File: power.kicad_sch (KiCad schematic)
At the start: 38 parts, among them J2 Power, U3 TLV62569DBV, U4 TLV62569DBV, U5 TLV62569DBV

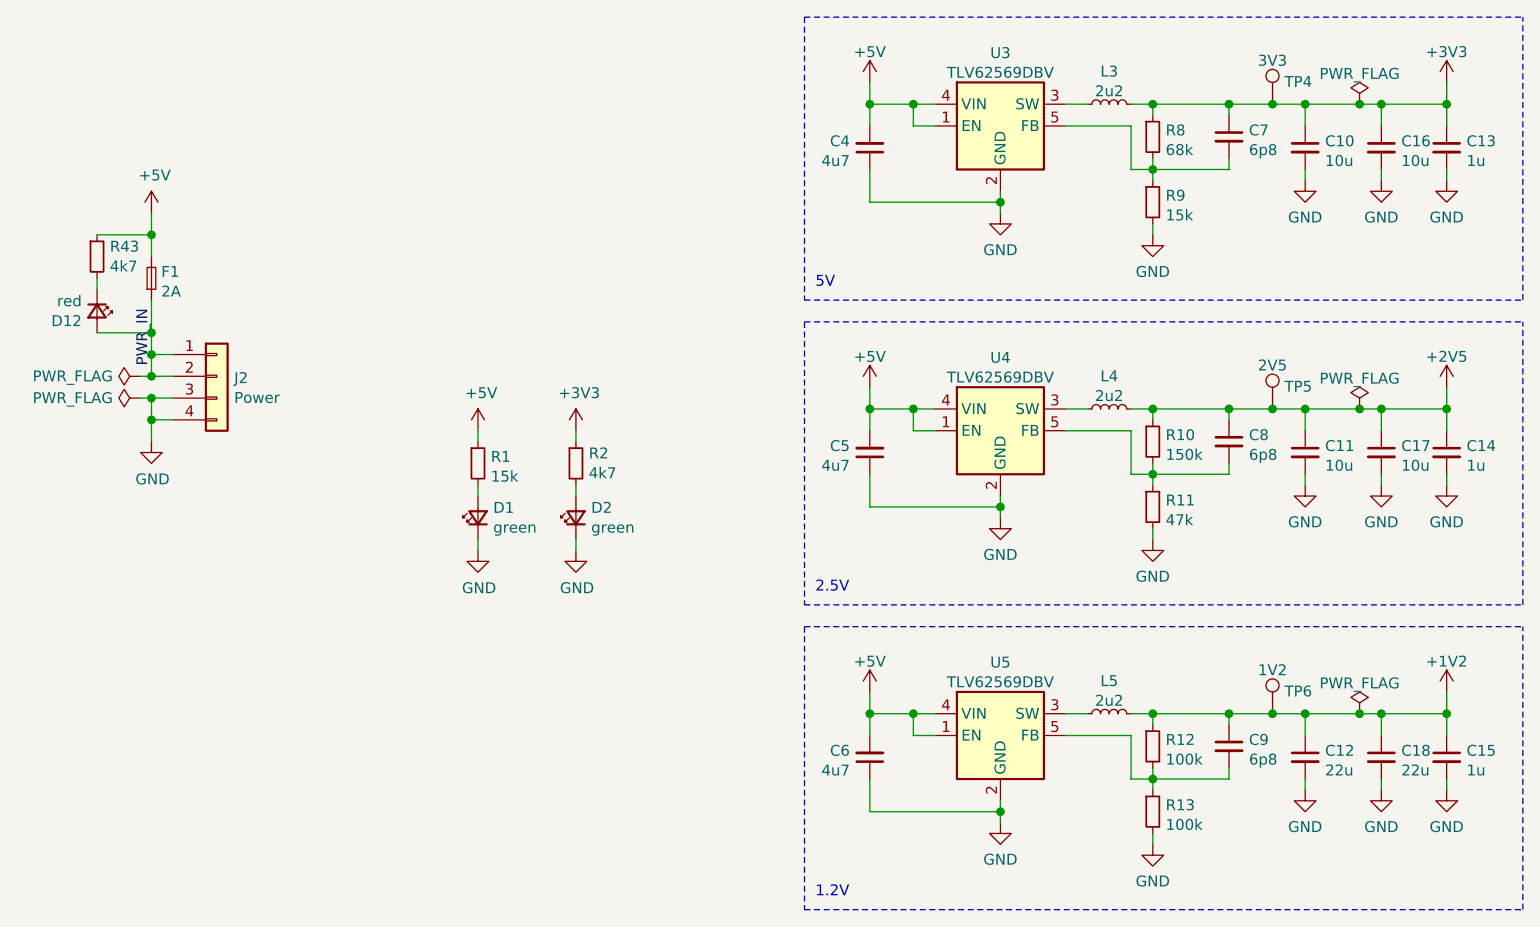
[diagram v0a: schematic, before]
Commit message: Update to KiCad 6
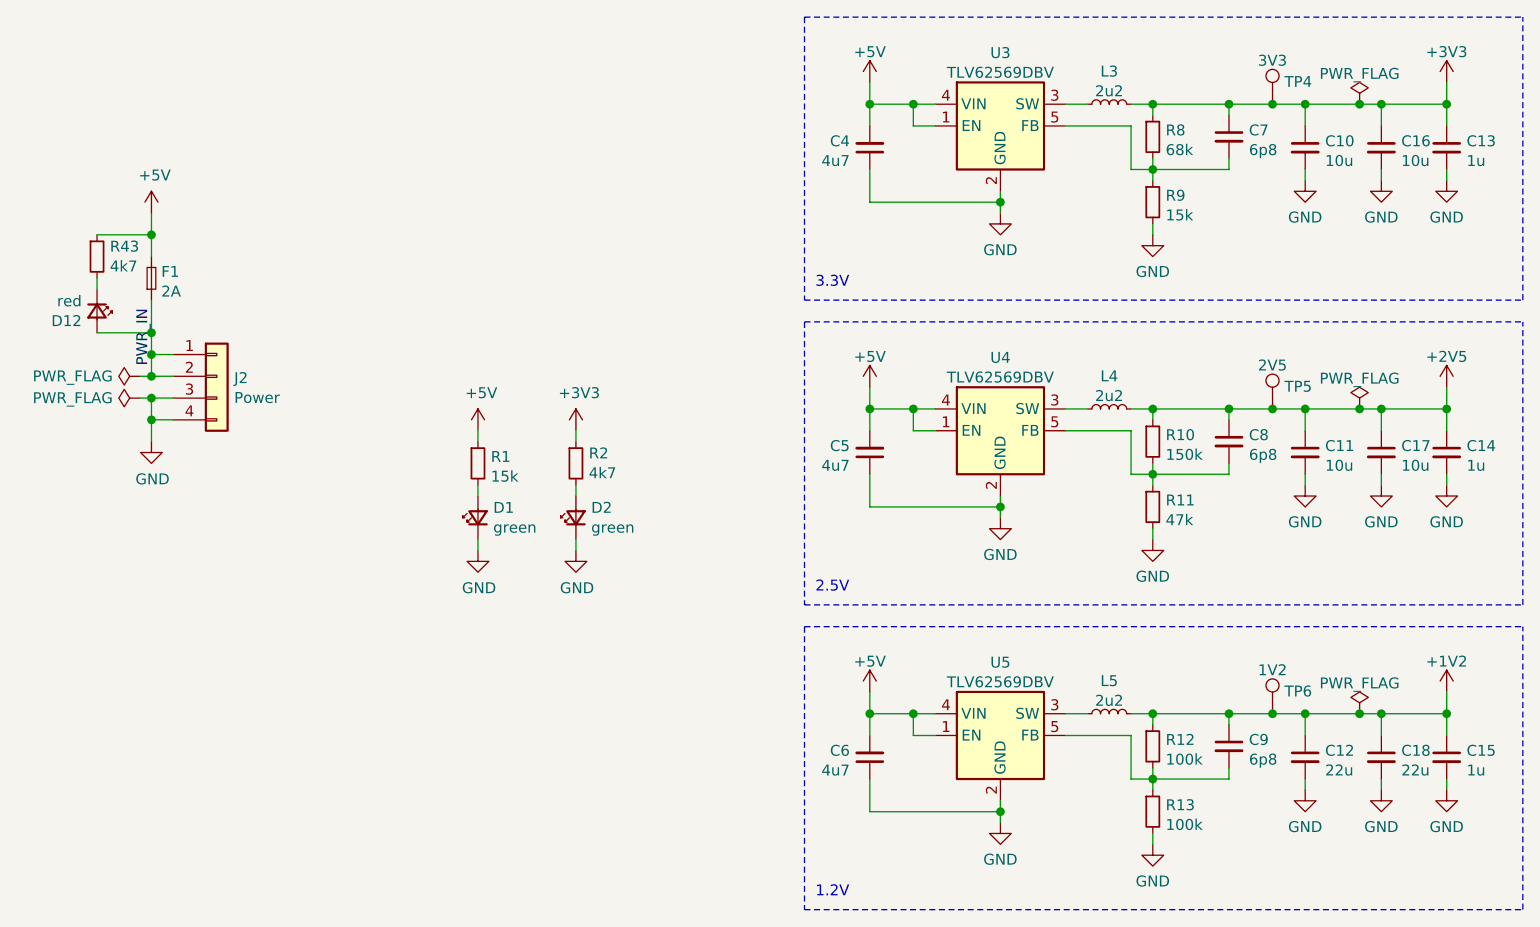
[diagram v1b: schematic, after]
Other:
- note added: "3.3V"
- note removed: "5V"
